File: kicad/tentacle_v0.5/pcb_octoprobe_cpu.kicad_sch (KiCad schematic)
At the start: 28 parts, among them J201 Conn_02x05, U201 RP2040, U202 AMS1117-3.3, U203 W25Q32JVS, X201 Oscillator-12MHz

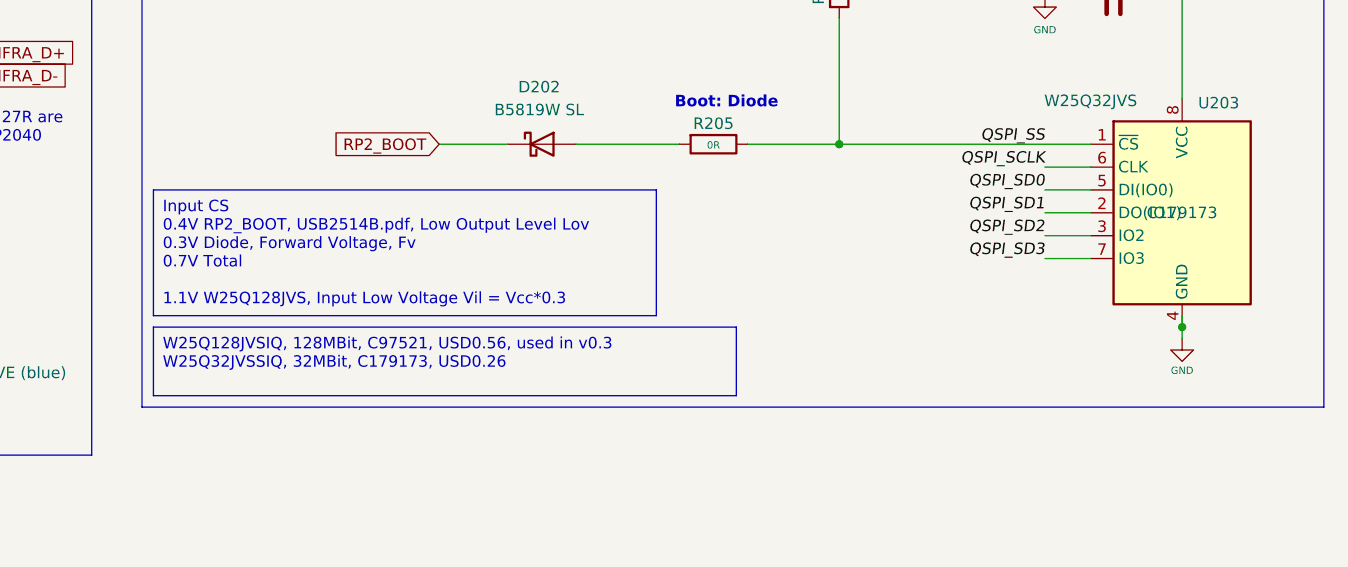
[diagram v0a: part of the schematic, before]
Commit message: Schematics: Fix ERC warnings
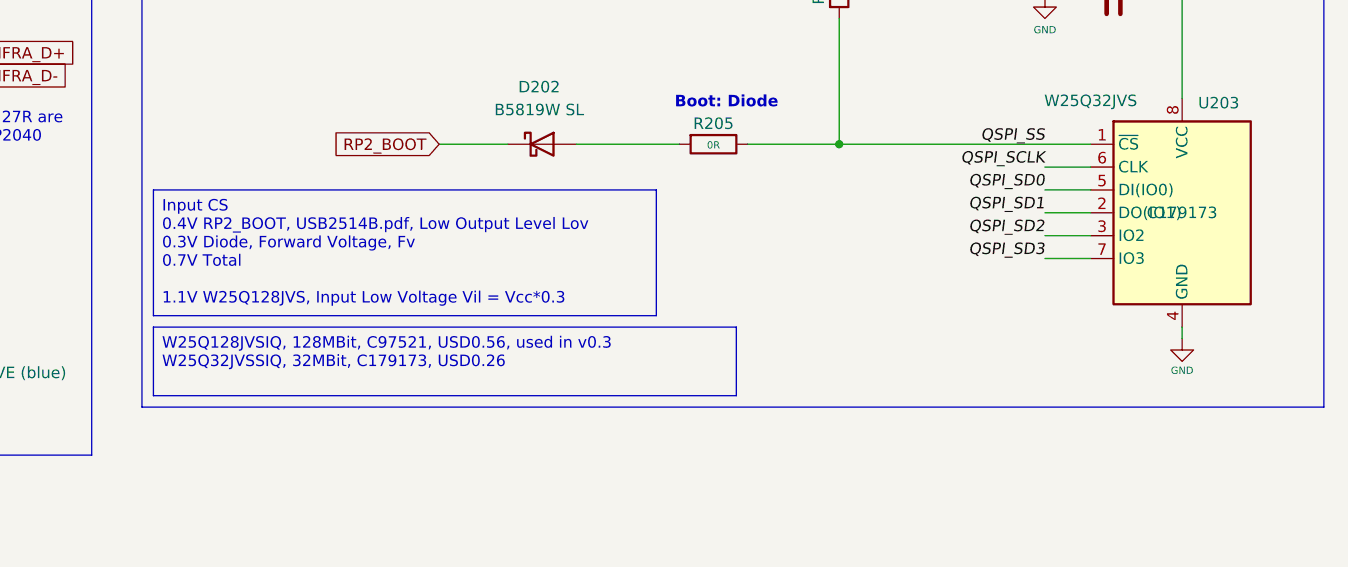
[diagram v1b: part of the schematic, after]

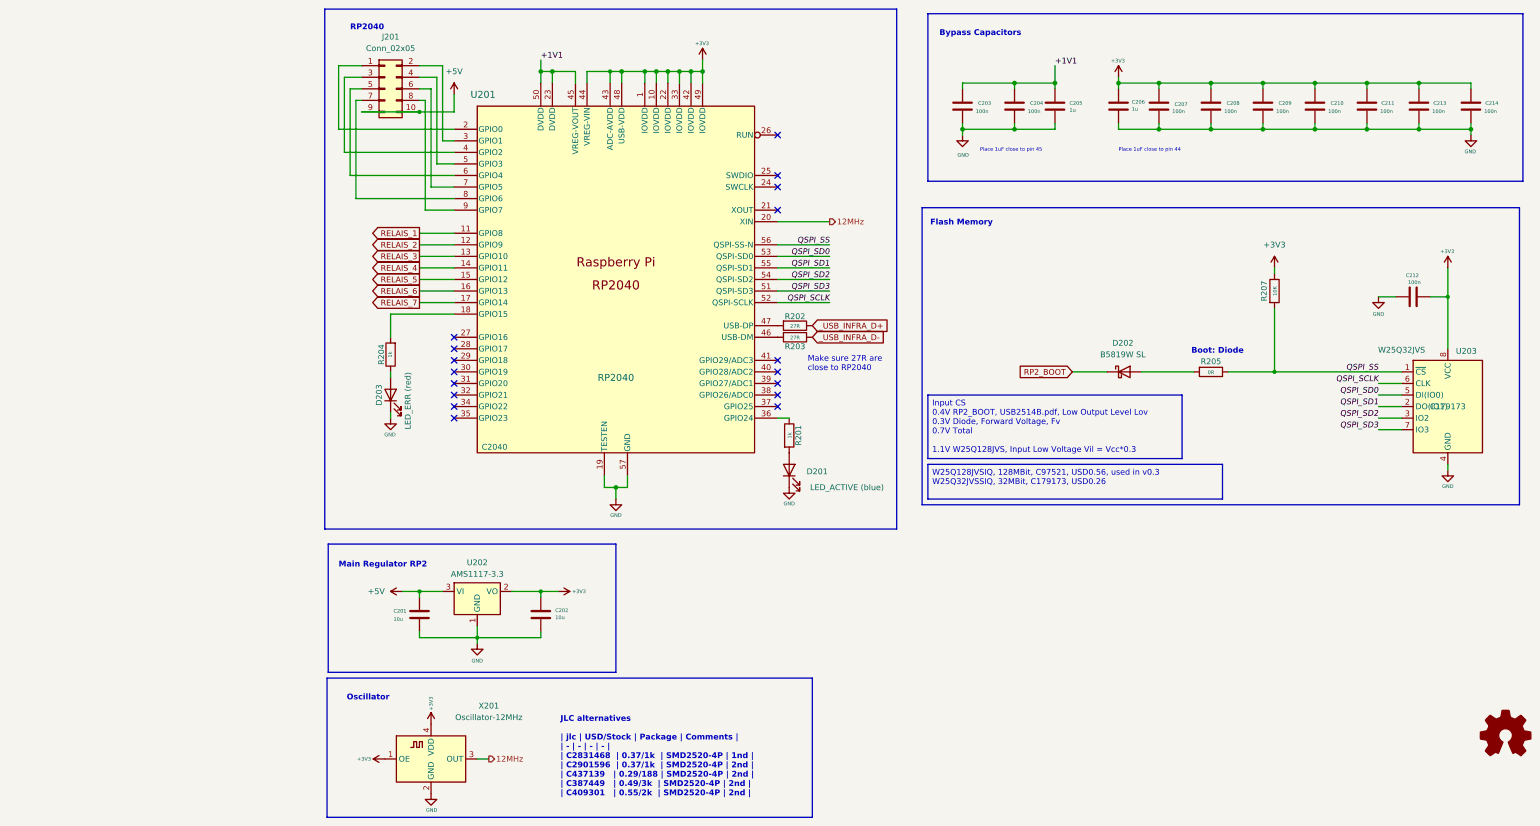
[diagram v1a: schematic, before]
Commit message: Breadboard: Remove pads from schematic
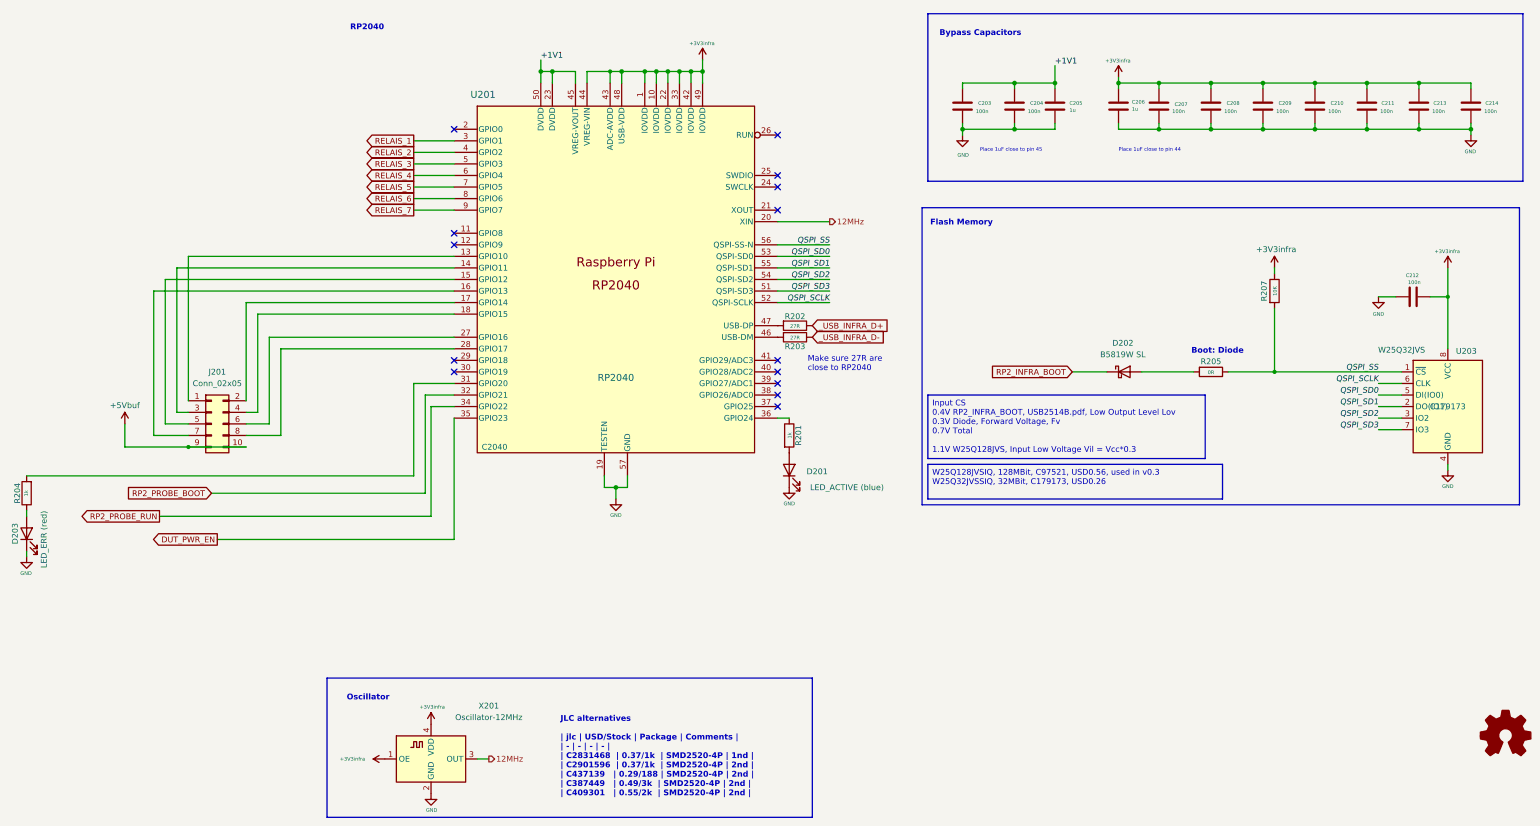
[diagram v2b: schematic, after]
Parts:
- removed C201, C202: 10u, Capacitor_SMD:C_0603_1608Metric, symbol 00_project_library:C
- removed U202: AMS1117-3.3, 00_project_library:SOT-223-3_TabPin2, symbol 00_project_library:AMS1117-3.3
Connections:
- net RELAIS_1: now also U201.3 (GPIO1); no longer U201.11 (GPIO8)
- net RELAIS_2: now also U201.4 (GPIO2); no longer U201.12 (GPIO9)
- net RELAIS_3: now also U201.5 (GPIO3); no longer U201.13 (GPIO10)
- net RELAIS_4: now also U201.6 (GPIO4); no longer U201.14 (GPIO11)
- net RELAIS_5: now also U201.7 (GPIO5); no longer U201.15 (GPIO12)
- net RELAIS_6: now also U201.8 (GPIO6); no longer U201.16 (GPIO13)
- net RELAIS_7: now also U201.9 (GPIO7); no longer U201.17 (GPIO14)
- net at J201.1 (Pin_1): now also U201.13 (GPIO10); no longer U201.2 (GPIO0)
- net at J201.2 (Pin_2): now also U201.17 (GPIO14); no longer U201.3 (GPIO1)
- net at J201.3 (Pin_3): now also U201.14 (GPIO11); no longer U201.4 (GPIO2)
- net at J201.4 (Pin_4): now also U201.18 (GPIO15); no longer U201.5 (GPIO3)
- net at J201.5 (Pin_5): now also U201.15 (GPIO12); no longer U201.6 (GPIO4)
- net at J201.6 (Pin_6): now also U201.27 (GPIO16); no longer U201.7 (GPIO5)
- net at J201.7 (Pin_7): now also U201.16 (GPIO13); no longer U201.8 (GPIO6)
- net at J201.8 (Pin_8): now also U201.28 (GPIO17); no longer U201.9 (GPIO7)
- net at R204.2: now also U201.31 (GPIO20); no longer U201.18 (GPIO15)
- net RP2_PROBE_BOOT: now reaches U201.32 (GPIO21)
- net RP2_PROBE_RUN: now reaches U201.34 (GPIO22)
- net DUT_PWR_EN: now reaches U201.35 (GPIO23)
- net +3V3 renamed +3V3infra
- net +5V renamed +5Vbuf
- net RP2_BOOT renamed RP2_INFRA_BOOT
- no-connect marks 17 -> 14
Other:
- note removed: "Main Regulator RP2"
- moved on the sheet: D203, J201, R204

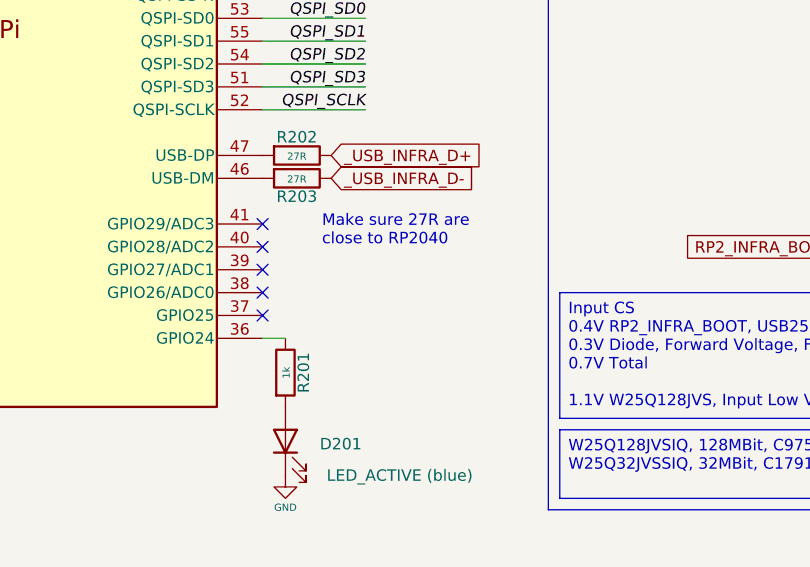
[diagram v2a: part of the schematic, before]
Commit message: ERC and DRC without errors and warnings LEDS less bright (Green LEDs 2k2 -> 4k7)
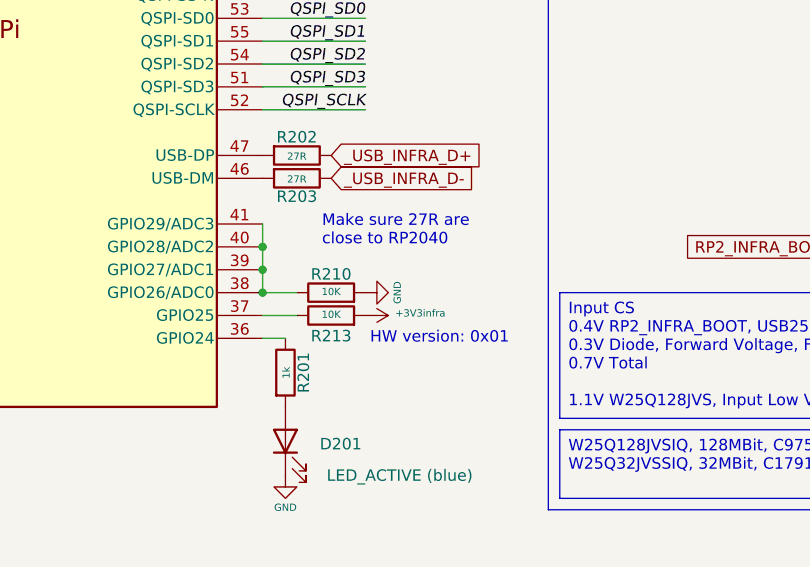
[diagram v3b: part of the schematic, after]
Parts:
- added R210, R213: 10K, Resistor_SMD:R_0402_1005Metric, symbol Device:R
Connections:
- net +3V3infra: now also R213.2
- net GND: now also R210.2
- net at U201.37 (GPIO25): now also R213.1
- net at U201.38 (GPIO26/ADC0): now also U201.39 (GPIO27/ADC1), U201.40 (GPIO28/ADC2), U201.41 (GPIO29/ADC3), R210.1
- no-connect marks 14 -> 9
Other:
- note added: "HW version: 0x01"

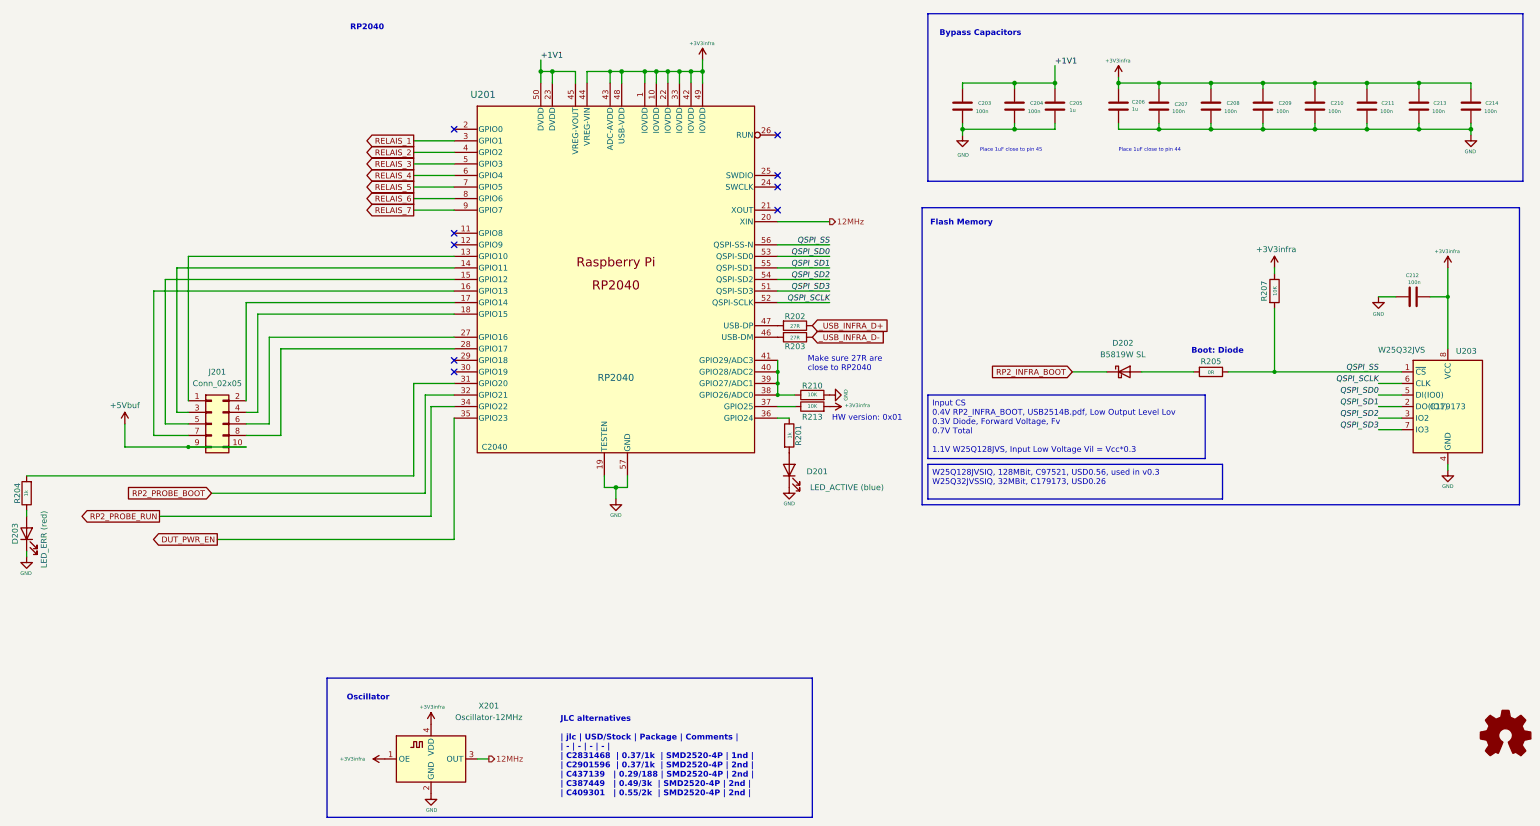
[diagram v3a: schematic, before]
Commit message: Ordered tentacle v0.5 at jlcpcb
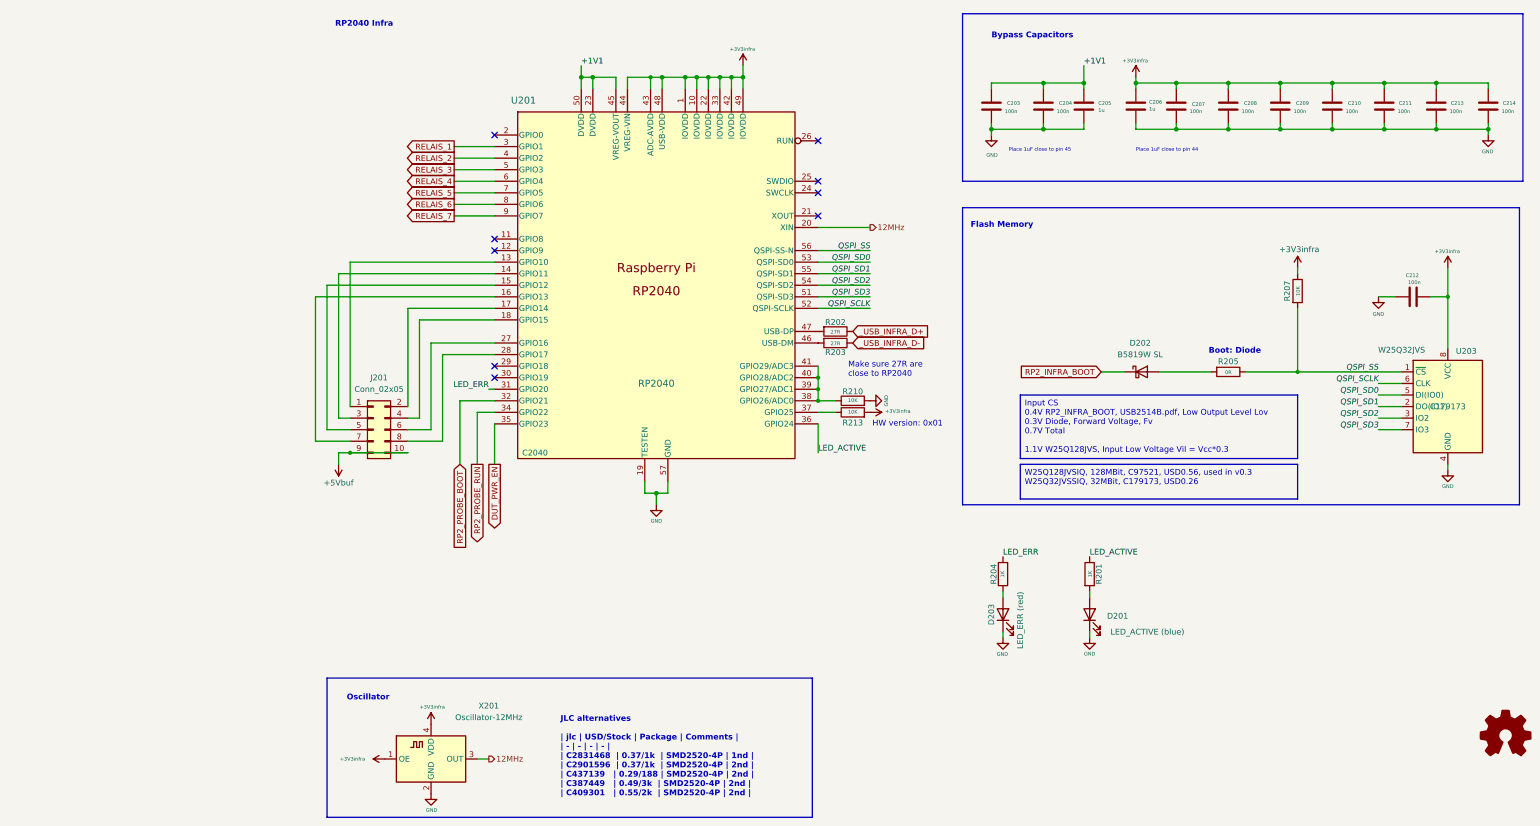
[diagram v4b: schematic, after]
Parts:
- R201, R204: value 1k -> 1K
- X201: footprint Oscillator:Oscillator_SMD_ECS_2520MV-xxx-xx-4Pin_2.5x2.0mm -> Crystal:Crystal_SMD_2520-4Pin_2.5x2.0mm; JLC C2831468 -> C2901596
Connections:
- net LED_ERR: now reaches R204.2, U201.31 (GPIO20)
- net LED_ACTIVE: now reaches R201.1, U201.36 (GPIO24)
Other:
- note added: "RP2040 Infra"
- note removed: "RP2040"
- moved on the sheet: C203, C204, C205, C206, C207, C208, C209, C210, C211, C213, C214, D201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

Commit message: tentacle v0.5 kicad - unknown small changes to schematics
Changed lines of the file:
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@@
 	)
 	(global_label "RP2_PROBE_BOOT"
-		(shape input)
+		(shape output)
 		(at 45.72 115.57 270)
 		(fields_autoplaced yes)
